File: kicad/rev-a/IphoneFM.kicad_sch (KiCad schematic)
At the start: 106 parts, among them J1 USB 2.0 Type-C, J2 SMA jack, SW1 SPDT, SW2 SPST, SW3 6 × SPST, U1 MCU, U2 Synthesizer, U3 3.3 V 600 mA LDO, U4 FM receiver, U5 SPDT RF switch, U6 USB ESD array, U7 Digital step attenuator, Y2 20 MHz CMOS XO

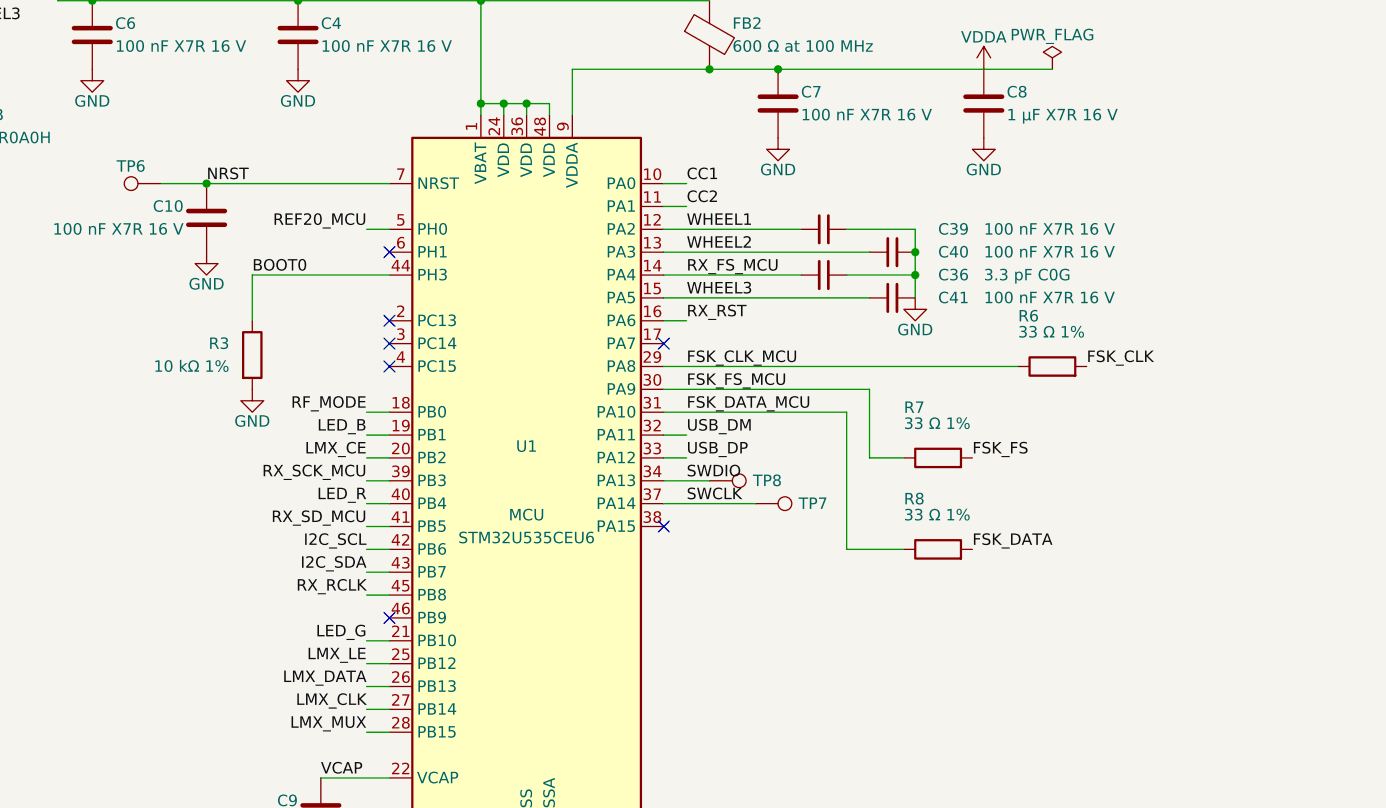
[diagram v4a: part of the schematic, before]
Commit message: U1 pins reassigned for the turned U1 of floorplan B3: receiver lines (PB6 FS, PB8 SCL, PB9 RCLK, PB4 RST) and U2 CE (PH1) on the U4/U2 sides, LEDs on PA0-PA2 (TIM2), wheels on PA3-PA5, RF_MODE PA7, CC on PB0/PB1; each checked against DS14217 Tables 26-28 and p132 and AN2606 Table 165; C36/C39/C40 follow their nets; U4 group 0.6 mm in from the edge
Co-Authored-By: Claude Opus 5.5 <noreply@anthropic.com>
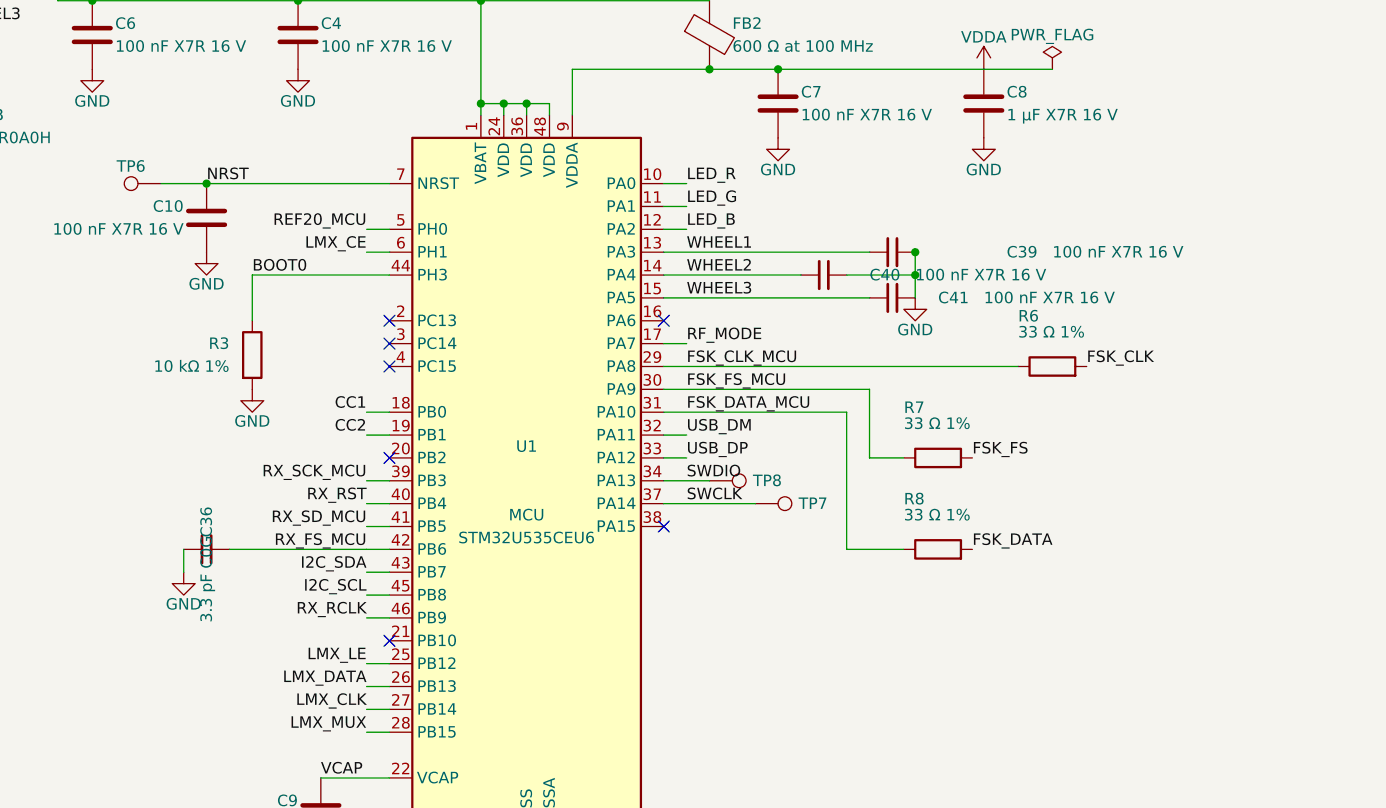
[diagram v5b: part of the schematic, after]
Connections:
- net CC1: now also U1.18 (PB0); no longer U1.10 (PA0)
- net CC2: now also U1.19 (PB1); no longer U1.11 (PA1)
- net I2C_SCL: now also U1.45 (PB8); no longer U1.42 (PB6)
- net LED_B: now also U1.12 (PA2); no longer U1.19 (PB1)
- net LED_G: now also U1.11 (PA1); no longer U1.21 (PB10)
- net LED_R: now also U1.10 (PA0); no longer U1.40 (PB4)
- net LMX_CE: now also U1.6 (PH1); no longer U1.20 (PB2)
- net RF_MODE: now also U1.17 (PA7); no longer U1.18 (PB0)
- net RX_FS_MCU: now also U1.42 (PB6); no longer U1.14 (PA4)
- net RX_RCLK: now also U1.46 (PB9); no longer U1.45 (PB8)
- net RX_RST: now also U1.40 (PB4); no longer U1.16 (PA6)
- net WHEEL1: now also U1.13 (PA3); no longer U1.12 (PA2)
- net WHEEL2: now also U1.14 (PA4); no longer U1.13 (PA3)
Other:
- moved on the sheet: C36, C39, C40
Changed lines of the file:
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@@
 	(symbol
 		(lib_id "Device:C_Small")
-		(at 256.54 228.60 90)
+		(at 187.96 259.08 270)
 		(unit 1)
 		(exclude_from_sim no)
@@
 		(dnp no)
 		(property "Reference" "C36"
-			(at 269.24 228.60 90)
-			(effects (font (size 1.27 1.27)) (justify right))
+			(at 187.96 256.03 0)
+			(effects (font (size 1.27 1.27)) )
 		)
 		(property "Value" "3.3 pF C0G"
-			(at 274.32 228.60 90)
-			(effects (font (size 1.27 1.27)) (justify right))
+			(at 187.96 262.38 0)
+			(effects (font (size 1.27 1.27)) )
 		)
 		(property "Footprint" "IphoneFM:C_0402_1005Metric"
-			(at 256.54 228.60 0)
+			(at 187.96 259.08 0)
 			(effects (font (size 1.27 1.27)) (hide yes))
 		)
 		(property "Datasheet" "~"
-			(at 256.54 228.60 0)
+			(at 187.96 259.08 0)
 			(effects (font (size 1.27 1.27)) (hide yes))
 		)
 		(property "MPN" "GRM1555C1H3R3CA01D"
-			(at 274.32 231.14 90)
+			(at 187.96 259.08 0)
 			(effects (font (size 1.27 1.27)) (hide yes))
 		)
 		(property "LCSC" "C76968"
-			(at 256.54 228.60 0)
+			(at 187.96 259.08 0)
 			(effects (font (size 1.27 1.27)) (hide yes))
 		)
 		(property "Manufacturer" "Murata"
-			(at 256.54 228.60 0)
+			(at 187.96 259.08 0)
 			(effects (font (size 1.27 1.27)) (hide yes))
 		)
@@
 	(symbol
 		(lib_id "Device:C_Small")
-		(at 256.54 223.52 90)
+		(at 264.16 226.06 90)
 		(unit 1)
 		(exclude_from_sim no)
@@
 		(dnp no)
 		(property "Reference" "C39"
-			(at 269.24 223.52 90)
+			(at 276.86 226.06 90)
 			(effects (font (size 1.27 1.27)) (justify right))
 		)
 		(property "Value" "100 nF X7R 16 V"
-			(at 274.32 223.52 90)
+			(at 281.94 226.06 90)
 			(effects (font (size 1.27 1.27)) (justify right))
 		)
 		(property "Footprint" "IphoneFM:C_0402_1005Metric"
-			(at 256.54 223.52 0)
+			(at 264.16 226.06 0)
 			(effects (font (size 1.27 1.27)) (hide yes))
 		)
 		(property "Datasheet" "~"
-			(at 256.54 223.52 0)
+			(at 264.16 226.06 0)
 			(effects (font (size 1.27 1.27)) (hide yes))
 		)
 		(property "MPN" "CL05B104KO5NNNC"
-			(at 274.32 226.06 90)
+			(at 281.94 228.60 90)
 			(effects (font (size 1.27 1.27)) (hide yes))
 		)
 		(property "LCSC" "C1525"
-			(at 256.54 223.52 0)
+			(at 264.16 226.06 0)
 			(effects (font (size 1.27 1.27)) (hide yes))
 		)
 		(property "Manufacturer" "Samsung"
-			(at 256.54 223.52 0)
+			(at 264.16 226.06 0)
 			(effects (font (size 1.27 1.27)) (hide yes))
 		)
@@
 	(symbol
 		(lib_id "Device:C_Small")
-		(at 264.16 226.06 90)
+		(at 256.54 228.60 90)
 		(unit 1)
 		(exclude_from_sim no)
@@
 		(dnp no)
 		(property "Reference" "C40"
-			(at 269.24 226.06 90)
+			(at 261.62 228.60 90)
 			(effects (font (size 1.27 1.27)) (justify right))
 		)
 		(property "Value" "100 nF X7R 16 V"
-			(at 274.32 226.06 90)
+			(at 266.70 228.60 90)
 			(effects (font (size 1.27 1.27)) (justify right))
 		)
 		(property "Footprint" "IphoneFM:C_0402_1005Metric"
-			(at 264.16 226.06 0)
+			(at 256.54 228.60 0)
 			(effects (font (size 1.27 1.27)) (hide yes))
 		)
 		(property "Datasheet" "~"
-			(at 264.16 226.06 0)
+			(at 256.54 228.60 0)
 			(effects (font (size 1.27 1.27)) (hide yes))
 		)
 		(property "MPN" "CL05B104KO5NNNC"
-			(at 274.32 228.60 90)
+			(at 266.70 231.14 90)
 			(effects (font (size 1.27 1.27)) (hide yes))
 		)
 		(property "LCSC" "C1525"
-			(at 264.16 226.06 0)
+			(at 256.54 228.60 0)
 			(effects (font (size 1.27 1.27)) (hide yes))
 		)
 		(property "Manufacturer" "Samsung"
-			(at 264.16 226.06 0)
+			(at 256.54 228.60 0)
 			(effects (font (size 1.27 1.27)) (hide yes))
 		)
@@
 	)
 	(wire
+		(pts (xy 205.74 259.08) (xy 190.50 259.08))
+		(stroke (width 0) (type default))
+	)
+	(wire
+		(pts (xy 185.42 259.08) (xy 185.42 261.62))
+		(stroke (width 0) (type default))
+	)
+	(wire
 		(pts (xy 223.52 292.10) (xy 223.52 294.64))
 		(stroke (width 0) (type default))
@@
 	(symbol
 		(lib_id "power:GND")
+		(at 185.42 261.62 0)
+		(unit 1)
+		(exclude_from_sim no)
+		(in_bom yes)
+		(on_board yes)
+		(dnp no)
+		(property "Reference" "#PWR103"
+			(at 185.42 261.62 0)
+			(effects (font (size 1.27 1.27)) (hide yes))
+		)
+		(property "Value" "GND"
+			(at 185.42 265.18 0)
+			(effects (font (size 1.27 1.27)))
+		)
+		(property "Footprint" ""
+			(at 185.42 261.62 0)
+			(effects (font (size 1.27 1.27)) (hide yes))
+		)
+		(property "Datasheet" ""
+			(at 185.42 261.62 0)
+			(effects (font (size 1.27 1.27)) (hide yes))
+		)
+		(pin "1"
+		)
+		(instances
+			(project "IphoneFM"
+				(path "/efee88c9-028d-4fdb-86e0-0a4145b330e1"
+					(reference "#PWR103") (unit 1)
+				)
+			)
+		)
+	)
+	(symbol
+		(lib_id "power:GND")
 		(at 322.58 88.90 270)
 		(unit 1)
@@
 	)
 	(wire
-		(pts (xy 238.76 223.52) (xy 254.00 223.52))
+		(pts (xy 238.76 223.52) (xy 241.30 223.52))
 		(stroke (width 0) (type default))
 	)
@@
 		(stroke (width 0) (type default))
 	)
-	(wire
-		(pts (xy 259.08 223.52) (xy 266.70 223.52))
-		(stroke (width 0) (type default))
-	)
-	(wire
-		(pts (xy 266.70 223.52) (xy 266.70 226.06))
-		(stroke (width 0) (type default))
-	)
 	(junction
 		(at 266.70 228.60)
@@
 		(stroke (width 0) (type default))
 	)
-	(label "CC1"
+	(label "LED_R"
 		(at 241.30 218.44 0)
 		(effects (font (size 1.27 1.27)) (justify left bottom))
@@
 		(stroke (width 0) (type default))
 	)
-	(label "CC2"
+	(label "LED_G"
 		(at 241.30 220.98 0)
 		(effects (font (size 1.27 1.27)) (justify left bottom))
@@
 		(stroke (width 0) (type default))
 	)
-	(label "I2C_SCL"
+	(label "RX_FS_MCU"
 		(at 205.74 259.08 180)
 		(effects (font (size 1.27 1.27)) (justify right bottom))
@@
 		(stroke (width 0) (type default))
 	)
-	(label "LED_B"
+	(label "CC2"
 		(at 205.74 246.38 180)
 		(effects (font (size 1.27 1.27)) (justify right bottom))
@@
 	)
 	(wire
-		(pts (xy 208.28 269.24) (xy 205.74 269.24))
+		(pts (xy 208.28 266.70) (xy 205.74 266.70))
 		(stroke (width 0) (type default))
 	)
-	(label "LED_G"
-		(at 205.74 269.24 180)
+	(label "RX_RCLK"
+		(at 205.74 266.70 180)
 		(effects (font (size 1.27 1.27)) (justify right bottom))
 	)
@@
 		(stroke (width 0) (type default))
 	)
-	(label "LED_R"
+	(label "RX_RST"
 		(at 205.74 254.00 180)
 		(effects (font (size 1.27 1.27)) (justify right bottom))
 	)
 	(wire
-		(pts (xy 208.28 248.92) (xy 205.74 248.92))
+		(pts (xy 208.28 226.06) (xy 205.74 226.06))
 		(stroke (width 0) (type default))
 	)
 	(label "LMX_CE"
-		(at 205.74 248.92 180)
+		(at 205.74 226.06 180)
 		(effects (font (size 1.27 1.27)) (justify right bottom))
 	)
@@
 		(stroke (width 0) (type default))
 	)
-	(label "RF_MODE"
+	(label "CC1"
 		(at 205.74 243.84 180)
 		(effects (font (size 1.27 1.27)) (justify right bottom))
@@
 		(stroke (width 0) (type default))
 	)
-	(label "RX_RCLK"
+	(label "I2C_SCL"
 		(at 205.74 264.16 180)
 		(effects (font (size 1.27 1.27)) (justify right bottom))
@@
 	)
 	(wire
-		(pts (xy 238.76 233.68) (xy 241.30 233.68))
+		(pts (xy 238.76 236.22) (xy 241.30 236.22))
 		(stroke (width 0) (type default))
 	)
-	(label "RX_RST"
-		(at 241.30 233.68 0)
+	(label "RF_MODE"
+		(at 241.30 236.22 0)
 		(effects (font (size 1.27 1.27)) (justify left bottom))
 	)
@@
 		(effects (font (size 1.27 1.27)) (justify left bottom))
 	)
-	(label "RX_FS_MCU"
+	(label "WHEEL2"
 		(at 241.30 228.60 0)
 		(effects (font (size 1.27 1.27)) (justify left bottom))
@@
 		(effects (font (size 1.27 1.27)) (justify left bottom))
 	)
-	(label "WHEEL1"
+	(label "LED_B"
 		(at 241.30 223.52 0)
 		(effects (font (size 1.27 1.27)) (justify left bottom))
 	)
-	(label "WHEEL2"
+	(label "WHEEL1"
 		(at 241.30 226.06 0)
 		(effects (font (size 1.27 1.27)) (justify left bottom))
@@
 	)
 	(no_connect
-		(at 208.28 226.06)
+		(at 208.28 248.92)
 	)
 	(no_connect
-		(at 238.76 236.22)
+		(at 238.76 233.68)
 	)
 	(no_connect
@@
 	)
 	(no_connect
-		(at 208.28 266.70)
+		(at 208.28 269.24)
 	)
 	(no_connect

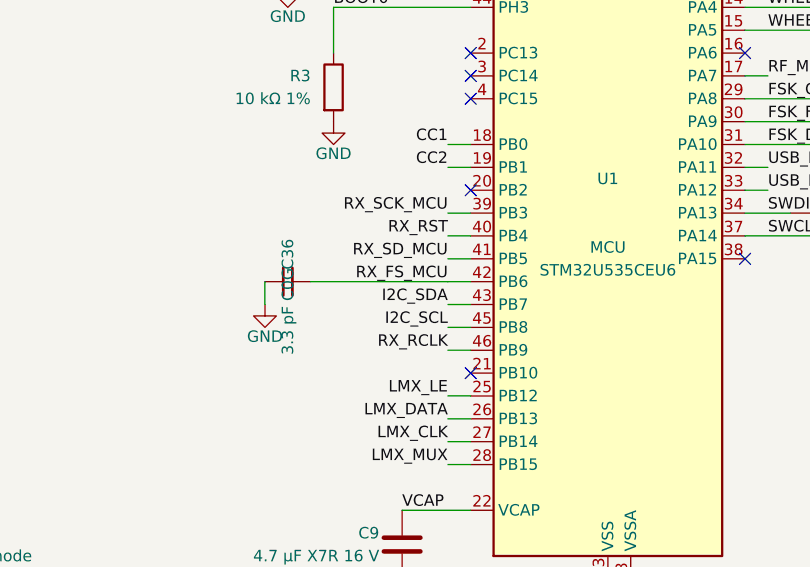
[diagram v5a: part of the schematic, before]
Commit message: Phase 5 prep: RX_RST to PB9 and RX_RCLK to PB4 (TIM3_CH1), U4 corner planned (pcb_route_u4.py) with U4's group 2.5 mm lower, U2 east caps re-stacked for CE, Y2/R4/C11/C12/R9/C5/C18/C19/TP7 and U3 group re-seated, C36 to R23 and R3 to SW2, lane plan rev 2
Co-Authored-By: Claude Opus 5.5 <noreply@anthropic.com>
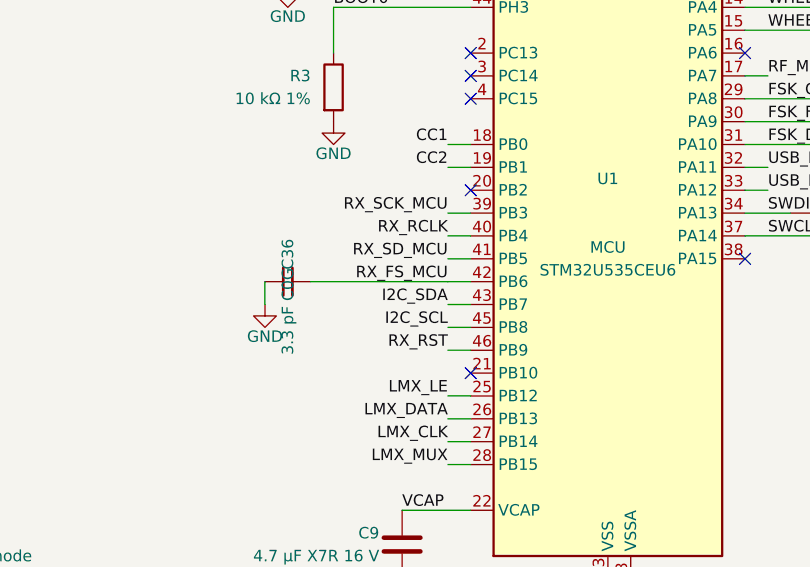
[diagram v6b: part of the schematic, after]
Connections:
- net RX_RCLK: now also U1.40 (PB4); no longer U1.46 (PB9)
- net RX_RST: now also U1.46 (PB9); no longer U1.40 (PB4)
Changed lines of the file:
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@@
 		(stroke (width 0) (type default))
 	)
-	(label "RX_RCLK"
+	(label "RX_RST"
 		(at 205.74 266.70 180)
 		(effects (font (size 1.27 1.27)) (justify right bottom))
@@
 		(stroke (width 0) (type default))
 	)
-	(label "RX_RST"
+	(label "RX_RCLK"
 		(at 205.74 254.00 180)
 		(effects (font (size 1.27 1.27)) (justify right bottom))

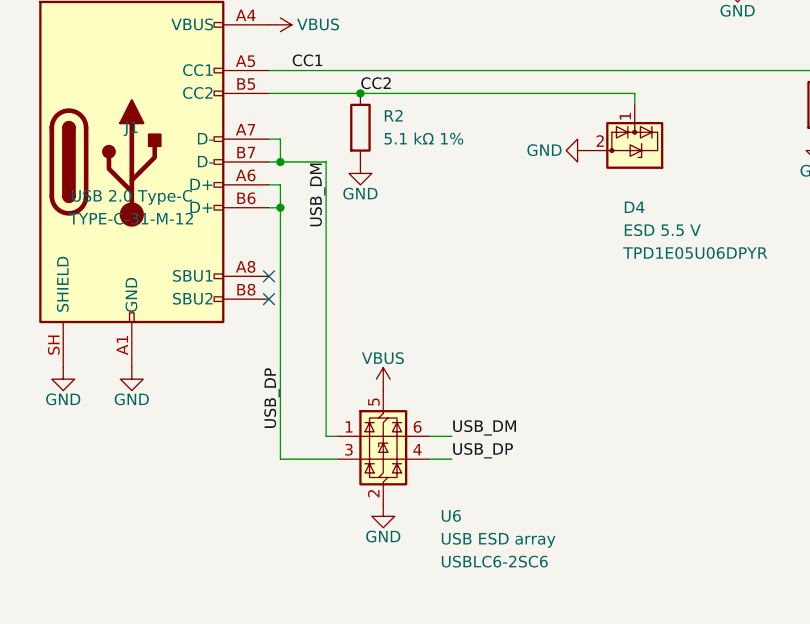
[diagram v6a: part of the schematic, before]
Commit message: Phase 5 prep: U1 escape at its new position, U2 plan (pcb_route_u2.py), U6 channels swapped
U1 sits at (36.135, 90.595) with its escape planned on all four sides; the U2 plan covers U2's
pins and parts (FSK with the clock hop, MICROWIRE, the PLL capacitor column, CE, REF20, 3V3
feeds), the USB pair under U2 up north of U6 (0.7 mm lower) and the two bottom 3V3 links in the
RF zone the user allowed (RF_BOTTOM_ALLOW). Checker: local pins now count branches; 0 findings
over the U1, U4, RF and U2 plans. U6's ESD channels swapped in the schematic and netlist.

Co-Authored-By: Claude Opus 5.5 <noreply@anthropic.com>
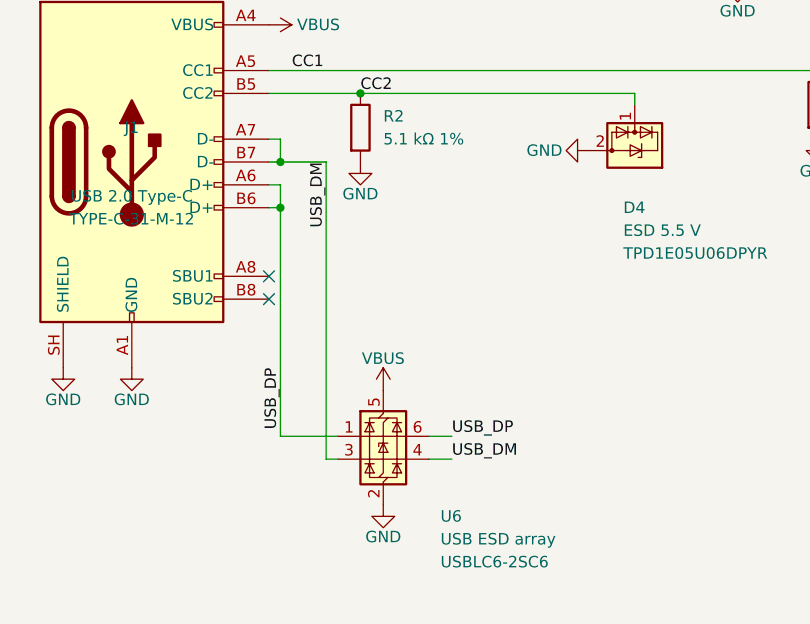
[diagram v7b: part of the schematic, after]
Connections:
- net USB_DM: now also U6.3 (I/O2), U6.4 (I/O2); no longer U6.1 (I/O1), U6.6 (I/O1)
- net USB_DP: now also U6.1 (I/O1), U6.6 (I/O1); no longer U6.3 (I/O2), U6.4 (I/O2)
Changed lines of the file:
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@@
 	)
 	(wire
-		(pts (xy 54.61 76.20) (xy 54.61 104.14))
+		(pts (xy 54.61 76.20) (xy 54.61 101.60))
 		(stroke (width 0) (type default))
 	)
@@
 	)
 	(wire
-		(pts (xy 60.96 104.14) (xy 54.61 104.14))
+		(pts (xy 54.61 101.60) (xy 60.96 101.60))
 		(stroke (width 0) (type default))
 	)
@@
 	)
 	(wire
-		(pts (xy 59.69 71.12) (xy 59.69 101.60))
+		(pts (xy 59.69 71.12) (xy 59.69 104.14))
 		(stroke (width 0) (type default))
 	)
@@
 	)
 	(wire
-		(pts (xy 60.96 101.60) (xy 59.69 101.60))
+		(pts (xy 59.69 104.14) (xy 60.96 104.14))
 		(stroke (width 0) (type default))
 	)
@@
 		(stroke (width 0) (type default))
 	)
-	(label "USB_DP"
+	(label "USB_DM"
 		(at 73.66 104.14 0)
 		(effects (font (size 1.27 1.27)) (justify left bottom))
@@
 		(stroke (width 0) (type default))
 	)
-	(label "USB_DM"
+	(label "USB_DP"
 		(at 73.66 101.60 0)
 		(effects (font (size 1.27 1.27)) (justify left bottom))

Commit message: JLC Basic-library parts for 14 passive types (same values and sizes, equal or higher ratings; datasheets saved); netlist, schematic, board, notes and wiring page updated
Co-Authored-By: Claude Opus 5.5 <noreply@anthropic.com>
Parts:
- C1, C2, C27, C8: value 1 µF X7R 16 V -> 1 µF X5R 50 V; LCSC C59782 -> C15849; MPN CL10B105KO8NNNC -> CL10A105KB8NNNC
- C12, C3: value 10 µF X5R 16 V -> 10 µF X5R 25 V; LCSC C1713 -> C15850; MPN CL21A106KOQNNNE -> CL21A106KAYNNNE
- C24, C26: LCSC C26409 -> C1546; MPN CL05C101JB5NNNC -> 0402CG101J500NT; Manufacturer Samsung -> FH
- C28, C30, C37, C38: LCSC C70465 -> C1562; MPN CL05C330JB5NNNC -> 0402CG330J500NT; Manufacturer Samsung -> FH
- C31, C34: value 1 nF C0G -> 1 nF X7R 50 V; LCSC C76947 -> C1523; MPN GRM1555C1H102JA01D -> 0402B102K500NT; Manufacturer Murata -> FH
- C32: LCSC C77023 -> C1532; MPN GRM155R71H223KA12D -> 0402B223K500NT; Manufacturer Murata -> FH
- C9: value 4.7 µF X7R 16 V -> 4.7 µF X5R 25 V; LCSC C408144 -> C1779; MPN GRM21BR71C475KE51L -> CL21A475KAQNNNE; Manufacturer Murata -> Samsung
- R1, R2: LCSC C105872 -> C25905; MPN RC0402FR-075K1L -> 0402WGF5101TCE; Manufacturer Yageo -> UNI-ROYAL
- R10, R11, R12, R13, R14, R15, R19, R3, R9: LCSC C60490 -> C25744; MPN RC0402FR-0710KL -> 0402WGF1002TCE; Manufacturer Yageo -> UNI-ROYAL
- R16, R17: LCSC C106235 -> C11702; MPN RC0402FR-071KL -> 0402WGF1001TCE; Manufacturer Yageo -> UNI-ROYAL
- R18: LCSC C60491 -> C25741; MPN RC0402FR-07100KL -> 0402WGF1003TCE; Manufacturer Yageo -> UNI-ROYAL
- R23, R24: LCSC C413086 -> C4109; MPN ERJ-2RKF2001X -> 0402WGF2001TCE; Manufacturer Panasonic -> UNI-ROYAL
- R25: LCSC C276273 -> C25123; MPN RC0402FR-07510RL -> 0402WGF5100TCE; Manufacturer Yageo -> UNI-ROYAL
- R4, R6, R7, R8: LCSC C138002 -> C25105; MPN RC0402FR-0733RL -> 0402WGF330JTCE; Manufacturer Yageo -> UNI-ROYAL
